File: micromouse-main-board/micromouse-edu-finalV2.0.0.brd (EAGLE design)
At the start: 93.9 x 75 mm, 113 parts, among them IC1 LM321MFX, J3 HTSS-103-XX-XX-D, J5 HTSS-103-XX-XX-D, J6 HTSS-102-XX-XX-D, J7 HTSS-102-XX-XX-D, U1 SN74HC151DR, U2 DRV8848PWPR, U3 ACS712ELCTR-20A-T, U6 MPU-6000, X1 RASPI_GPIO_B+#_PIN

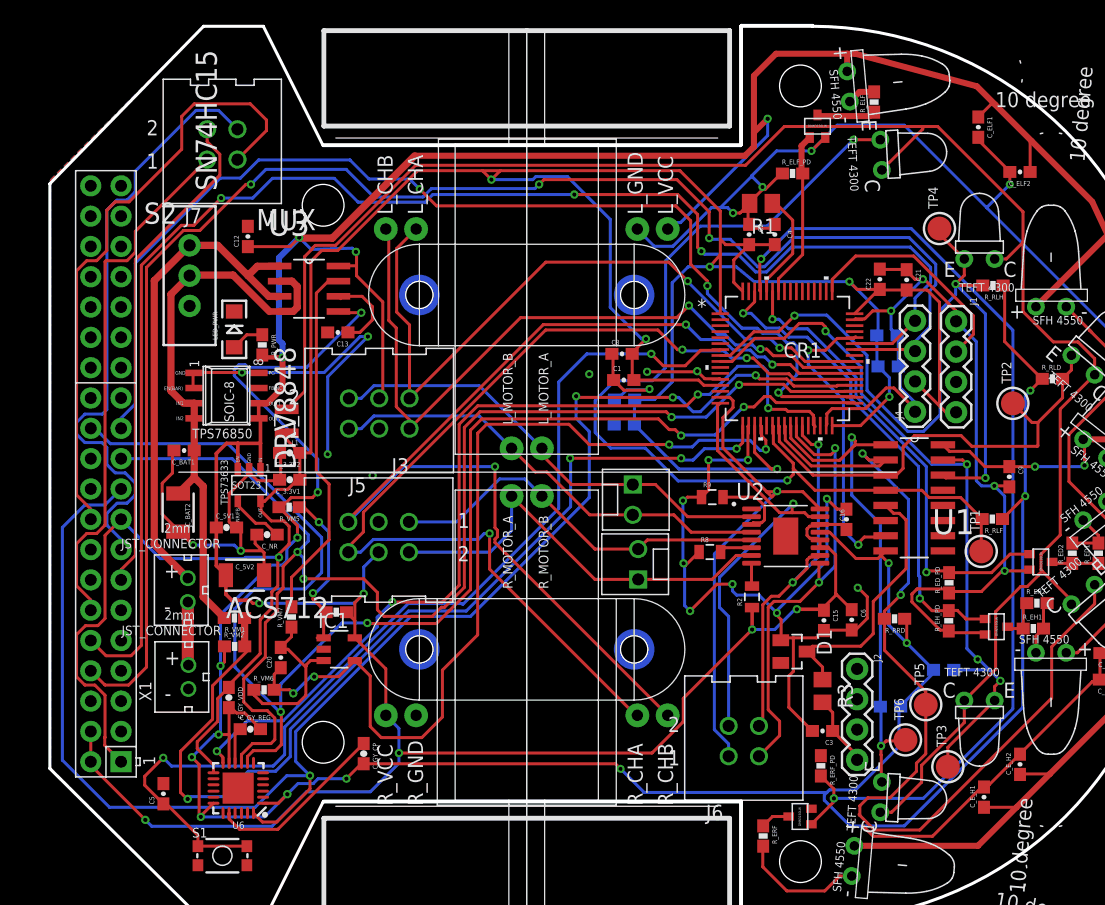
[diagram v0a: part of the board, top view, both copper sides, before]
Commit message: value update to reflect bom
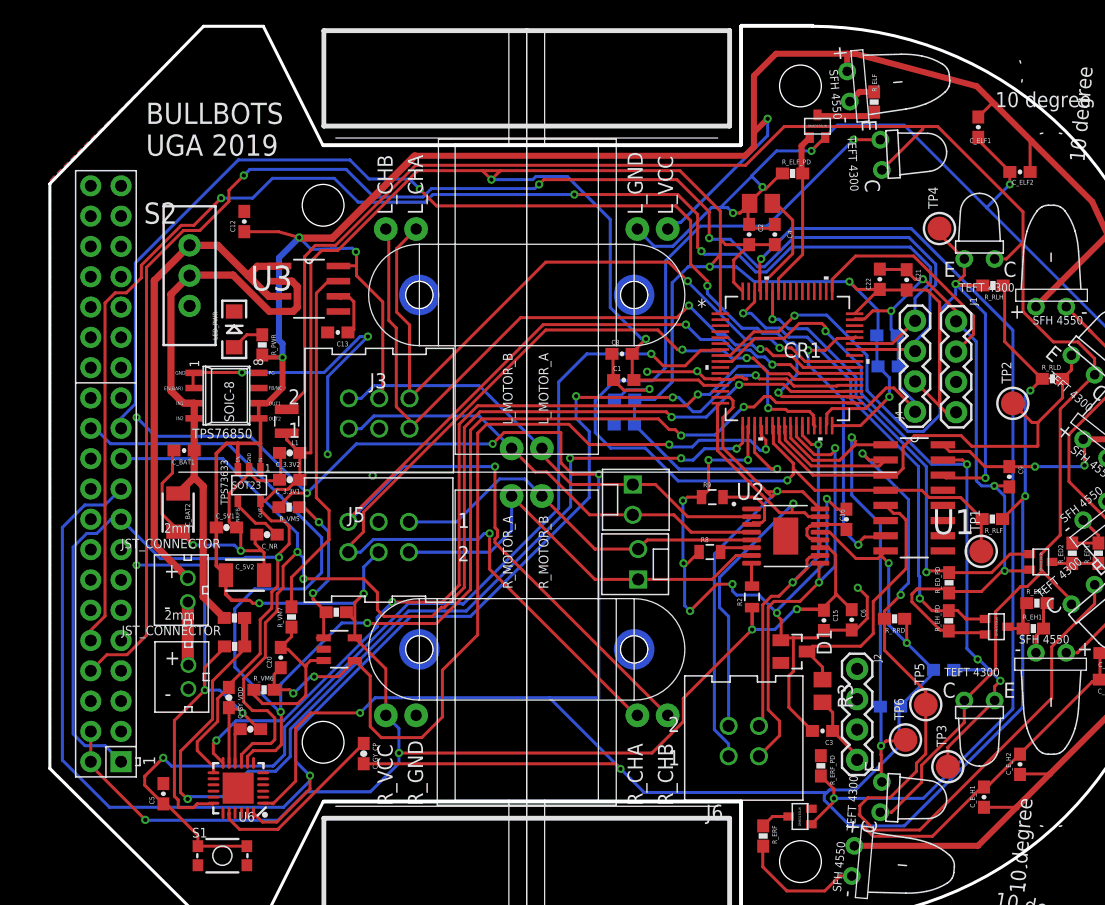
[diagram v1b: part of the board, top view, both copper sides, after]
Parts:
- removed J7: HTSS-102-XX-XX-D, HTSS-102-01-G-D:HTSS-102-XX-XX-D
- C4: value 0.1uF -> 0.01uF
- R_VM2: value 25k -> 33k
- moved C12 1.29 mm to (8.39, 58.6)
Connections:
- removed net GPIO_BREAKOUT_1: J7.2, X1.13
- removed net GPIO_BREAKOUT_2: J7.4, X1.15
- removed net PWM_BREAKOUT_1: J7.1, X1.12
- removed net PWM_BREAKOUT_2: J7.3, X1.18
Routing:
- net AGND: track 231.4 -> 307.9 mm, vias 14 -> 13
- net GPIO_BREAKOUT_2: track 51.8 -> 0.00 mm
- net PWM_BREAKOUT_2: track 51.5 -> 0.00 mm
- net PWM_BREAKOUT_1: track 44.3 -> 0.00 mm
- net GPIO_BREAKOUT_1: track 41.6 -> 0.00 mm
- net (USART1)_TX: track 124.0 -> 120.7 mm
- net GND: track 336.5 -> 339.2 mm, vias 27 -> 26
- net N$1: track 7.08 -> 4.68 mm
- net (USART1)_RX: track 129.8 -> 127.8 mm
- net SPI2_MISO: track 110.9 -> 109.7 mm
- net 3.3V: track 277.2 -> 278.3 mm
- net INT: track 77.4 -> 78.2 mm
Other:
- board text added: "BULLBOTS UGA 2019"
- board text removed: "ACS712"
- board text removed: "DRV8848"
- board text removed: "MUX"
- board text removed: "SN74HC15"
